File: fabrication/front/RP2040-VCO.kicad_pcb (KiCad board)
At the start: 2 copper layers, 20 x 128.5 mm, 2 parts

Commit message: update to v1.1
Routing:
- added copper zone on B.Cu, net GND
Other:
- board text added: "RP2040 VCO V1.1 BleepSound 2023"

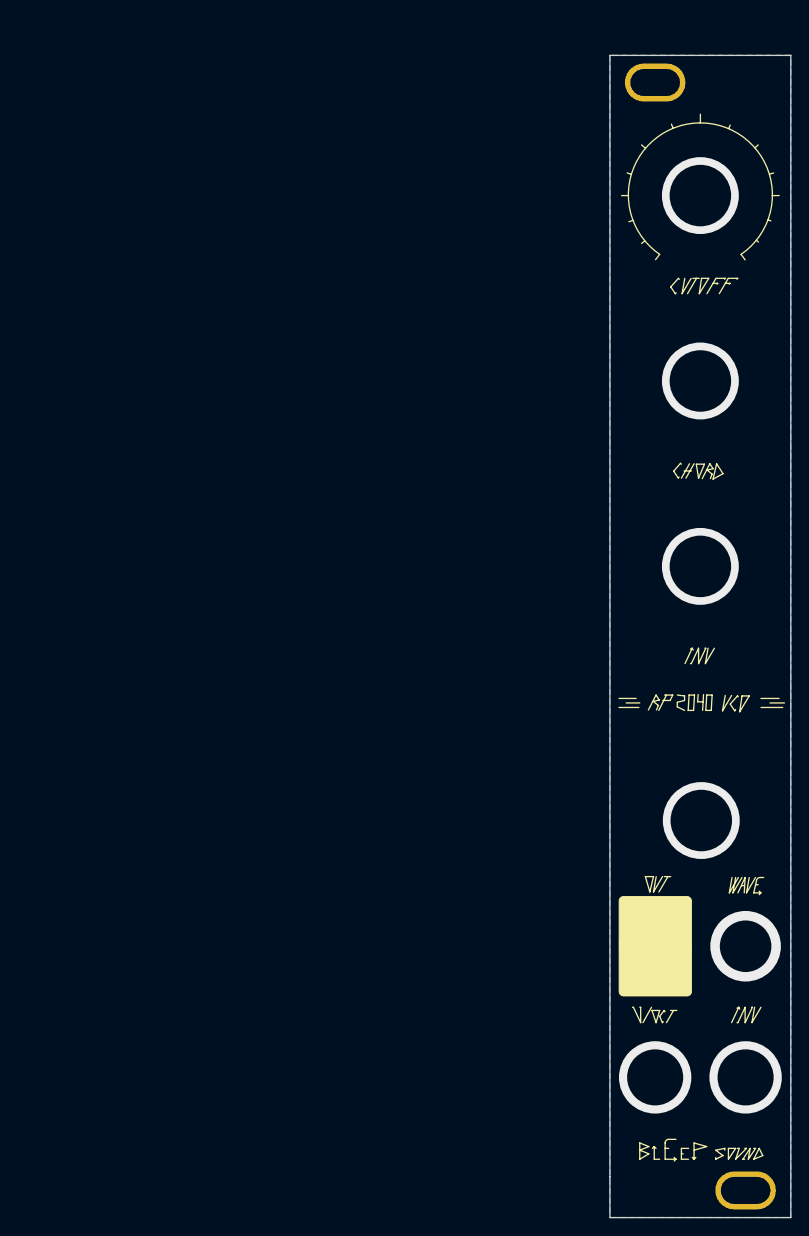
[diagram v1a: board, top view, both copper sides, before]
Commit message: update label for tune (fix issue)
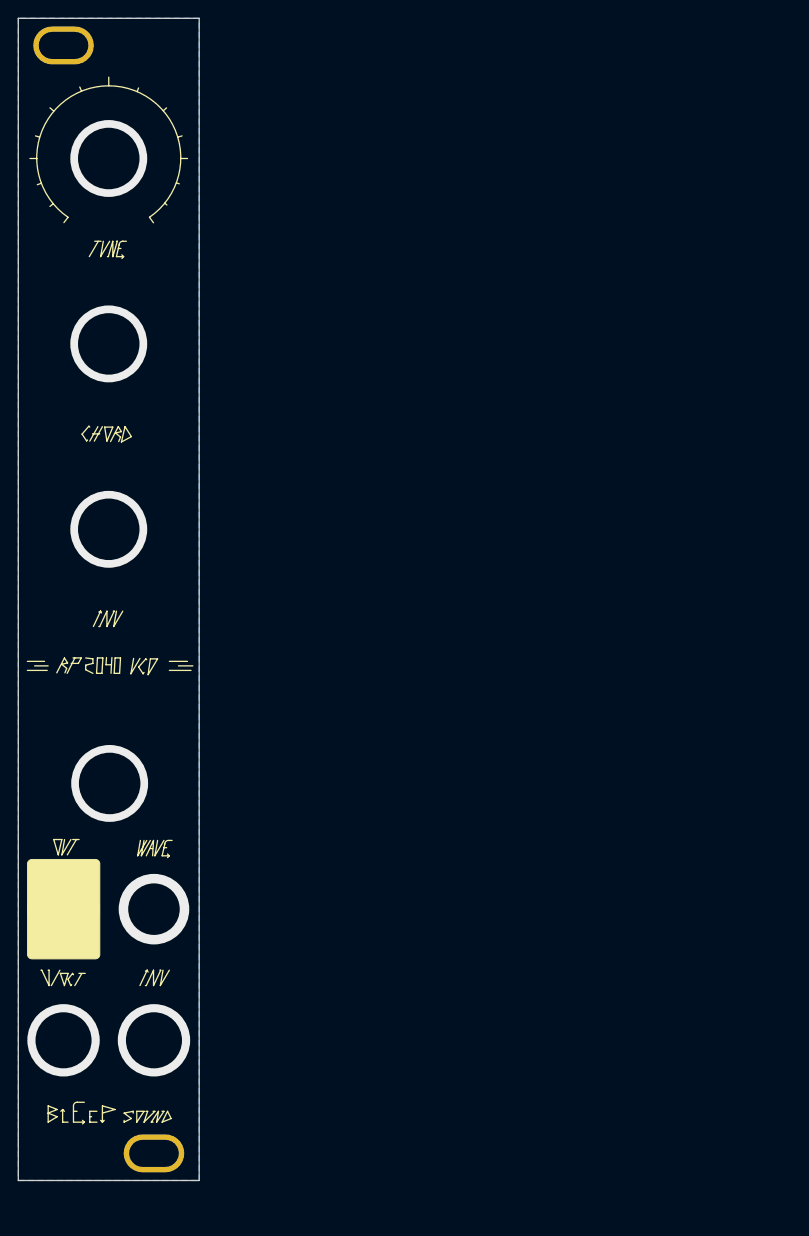
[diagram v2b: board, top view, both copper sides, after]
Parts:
- moved H3 65.5 mm to (51.1, 25.9)
- moved H4 65.5 mm to (61.1, 148.4)
- renumbered H1 to H3
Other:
- board text removed: "RP2040 VCO V1.0 BleepSound 2023"

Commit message: update fab files and repo organization
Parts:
- moved H3 65.5 mm to (116.5, 30.0)
- moved H4 65.5 mm to (126.5, 152.5)
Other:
- board text added: "RP2040 VCO V1.2 BleepSound 2023"
- board text removed: "RP2040 VCO V1.1 BleepSound 2023"

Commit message: V1.4 update
add extra 10k resistor on inv CV input (missing)
Update BoM for clarity
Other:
- board text added: "RP2040 VCO V1.4 BleepSound 2025"
- board text removed: "RP2040 VCO V1.2 BleepSound 2023"

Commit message: v1.5
reverse pots following issue raised on github
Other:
- board text added: "RP2040 VCO V1.5 BleepSound 2025"
- board text removed: "RP2040 VCO V1.4 BleepSound 2025"
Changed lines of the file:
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@@
 (kicad_pcb
-	(version 20240108)
+	(version 20241229)
 	(generator "pcbnew")
-	(generator_version "8.0")
+	(generator_version "9.0")
 	(general
 		(thickness 1.6)
@@
 	(layers
 		(0 "F.Cu" signal)
-		(31 "B.Cu" signal)
-		(32 "B.Adhes" user "B.Adhesive")
-		(33 "F.Adhes" user "F.Adhesive")
-		(34 "B.Paste" user)
-		(35 "F.Paste" user)
-		(36 "B.SilkS" user "B.Silkscreen")
-		(37 "F.SilkS" user "F.Silkscreen")
-		(38 "B.Mask" user)
-		(39 "F.Mask" user)
-		(40 "Dwgs.User" user "User.Drawings")
-		(41 "Cmts.User" user "User.Comments")
-		(42 "Eco1.User" user "User.Eco1")
-		(43 "Eco2.User" user "User.Eco2")
-		(44 "Edge.Cuts" user)
-		(45 "Margin" user)
-		(46 "B.CrtYd" user "B.Courtyard")
-		(47 "F.CrtYd" user "F.Courtyard")
-		(48 "B.Fab" user)
-		(49 "F.Fab" user)
+		(2 "B.Cu" signal)
+		(9 "F.Adhes" user "F.Adhesive")
+		(11 "B.Adhes" user "B.Adhesive")
+		(13 "F.Paste" user)
+		(15 "B.Paste" user)
+		(5 "F.SilkS" user "F.Silkscreen")
+		(7 "B.SilkS" user "B.Silkscreen")
+		(1 "F.Mask" user)
+		(3 "B.Mask" user)
+		(17 "Dwgs.User" user "User.Drawings")
+		(19 "Cmts.User" user "User.Comments")
+		(21 "Eco1.User" user "User.Eco1")
+		(23 "Eco2.User" user "User.Eco2")
+		(25 "Edge.Cuts" user)
+		(27 "Margin" user)
+		(31 "F.CrtYd" user "F.Courtyard")
+		(29 "B.CrtYd" user "B.Courtyard")
+		(35 "F.Fab" user)
+		(33 "B.Fab" user)
 	)
 	(setup
@@
 		(pad_to_mask_clearance 0)
 		(allow_soldermask_bridges_in_footprints no)
+		(tenting front back)
 		(pcbplotparams
-			(layerselection 0x00010fc_ffffffff)
-			(plot_on_all_layers_selection 0x0000000_00000000)
+			(layerselection 0x00000000_00000000_55555555_5755f5ff)
+			(plot_on_all_layers_selection 0x00000000_00000000_00000000_00000000)
 			(disableapertmacros no)
 			(usegerberextensions yes)
@@
 			(svgprecision 6)
 			(plotframeref no)
-			(viasonmask no)
 			(mode 1)
 			(useauxorigin no)
@@
 			(pdf_front_fp_property_popups yes)
 			(pdf_back_fp_property_popups yes)
+			(pdf_metadata yes)
+			(pdf_single_document no)
 			(dxfpolygonmode yes)
 			(dxfimperialunits yes)
@@
 			(psnegative no)
 			(psa4output no)
-			(plotreference yes)
-			(plotvalue no)
-			(plotfptext yes)
-			(plotinvisibletext no)
+			(plot_black_and_white yes)
 			(sketchpadsonfab no)
+			(plotpadnumbers no)
+			(hidednponfab no)
+			(sketchdnponfab yes)
+			(crossoutdnponfab yes)
 			(subtractmaskfromsilk yes)
 			(outputformat 1)
@@
 			)
 		)
-		(property "Footprint" "Synth:Doepfer Mounting hole"
-			(at 0 0 0)
-			(layer "F.Fab")
-			(hide yes)
-			(effects
-				(font
-					(size 1.27 1.27)
-					(thickness 0.15)
-				)
-			)
-		)
-		(property "Datasheet" ""
+		(property "Datasheet" "~"
 			(at 0 0 0)
 			(layer "F.Fab")
@@
 			)
 		)
+		(property "Links" ""
+			(at 0 0 0)
+			(unlocked yes)
+			(layer "F.Fab")
+			(hide yes)
+			(effects
+				(font
+					(size 1 1)
+					(thickness 0.15)
+				)
+			)
+		)
 		(property ki_fp_filters "MountingHole*Pad*")
-		(sheetname "Racine")
+		(sheetname "/")
 		(sheetfile "RP2040-VCO.kicad_sch")
 		(attr through_hole exclude_from_bom)
@@
 			(pintype "input")
 		)
+		(embedded_fonts no)
 	)
 	(footprint "Synth:Doepfer Mounting hole"
@@
 			)
 		)
-		(property "Footprint" "Synth:Doepfer Mounting hole"
-			(at 0 0 0)
-			(layer "F.Fab")
-			(hide yes)
-			(effects
-				(font
-					(size 1.27 1.27)
-					(thickness 0.15)
-				)
-			)
-		)
-		(property "Datasheet" ""
+		(property "Datasheet" "~"
 			(at 0 0 0)
 			(layer "F.Fab")
@@
 			)
 		)
+		(property "Links" ""
+			(at 0 0 0)
+			(unlocked yes)
+			(layer "F.Fab")
+			(hide yes)
+			(effects
+				(font
+					(size 1 1)
+					(thickness 0.15)
+				)
+			)
+		)
 		(property ki_fp_filters "MountingHole*Pad*")
-		(sheetname "Racine")
+		(sheetname "/")
 		(sheetfile "RP2040-VCO.kicad_sch")
 		(attr through_hole exclude_from_bom)
@@
 			(pintype "input")
 		)
+		(embedded_fonts no)
 	)
 	(gr_line
@@
 			(type solid)
 		)
-		(fill none)
+		(fill no)
 		(layer "F.SilkS")
 	)
@@
 			(type solid)
 		)
-		(fill solid)
+		(fill yes)
 		(layer "F.SilkS")
 	)
@@
 			(type solid)
 		)
-		(fill solid)
+		(fill yes)
 		(layer "F.SilkS")
 	)
@@
 			(type solid)
 		)
-		(fill solid)
+		(fill yes)
 		(layer "F.SilkS")
 	)
@@
 			(type solid)
 		)
-		(fill solid)
+		(fill yes)
 		(layer "F.SilkS")
 	)
@@
 			(type solid)
 		)
-		(fill none)
+		(fill no)
 		(layer "F.SilkS")
 	)
@@
 			(type solid)
 		)
-		(fill none)
+		(fill no)
 		(layer "F.SilkS")
 	)
@@
 		)
 	)
-	(gr_text "RP2040 VCO\nV1.4 BleepSound\n2025"
+	(gr_text "RP2040 VCO\nV1.5 BleepSound\n2025"
 		(at 121.5 95.8 0)
 		(layer "B.SilkS")
@@
 		)
 		(height -2.5)
+		(format
+			(prefix "")
+			(suffix "")
+			(units 3)
+			(units_format 1)
+			(precision 4)
+		)
+		(style
+			(thickness 0.1)
+			(arrow_length 1.27)
+			(text_position_mode 0)
+			(arrow_direction outward)
+			(extension_height 0.58642)
+			(extension_offset 0.5)
+			(keep_text_aligned yes)
+		)
 		(gr_text "20,0000 mm"
 			(at 121.5 22.85 0)
@@
 			)
 		)
-		(format
-			(prefix "")
-			(suffix "")
-			(units 3)
-			(units_format 1)
-			(precision 4)
-		)
-		(style
-			(thickness 0.1)
-			(arrow_length 1.27)
-			(text_position_mode 0)
-			(extension_height 0.58642)
-			(extension_offset 0.5) keep_text_aligned)
 	)
 	(via
@@
 		)
 	)
+	(embedded_fonts no)
 )
